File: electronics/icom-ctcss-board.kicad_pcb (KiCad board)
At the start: 2 copper layers, 100 x 150 mm, 42 parts, among them J1 J_MIC_IN, J2 J_RADIO_OUT, J3 J_UI_ENCODER, J4 J_UI_LCD, J5 J_BYPASS, J6 J_UI_LEDS, Q1 2N3904RLRAG, U1 Teyleten USB-C 5V/16MHz

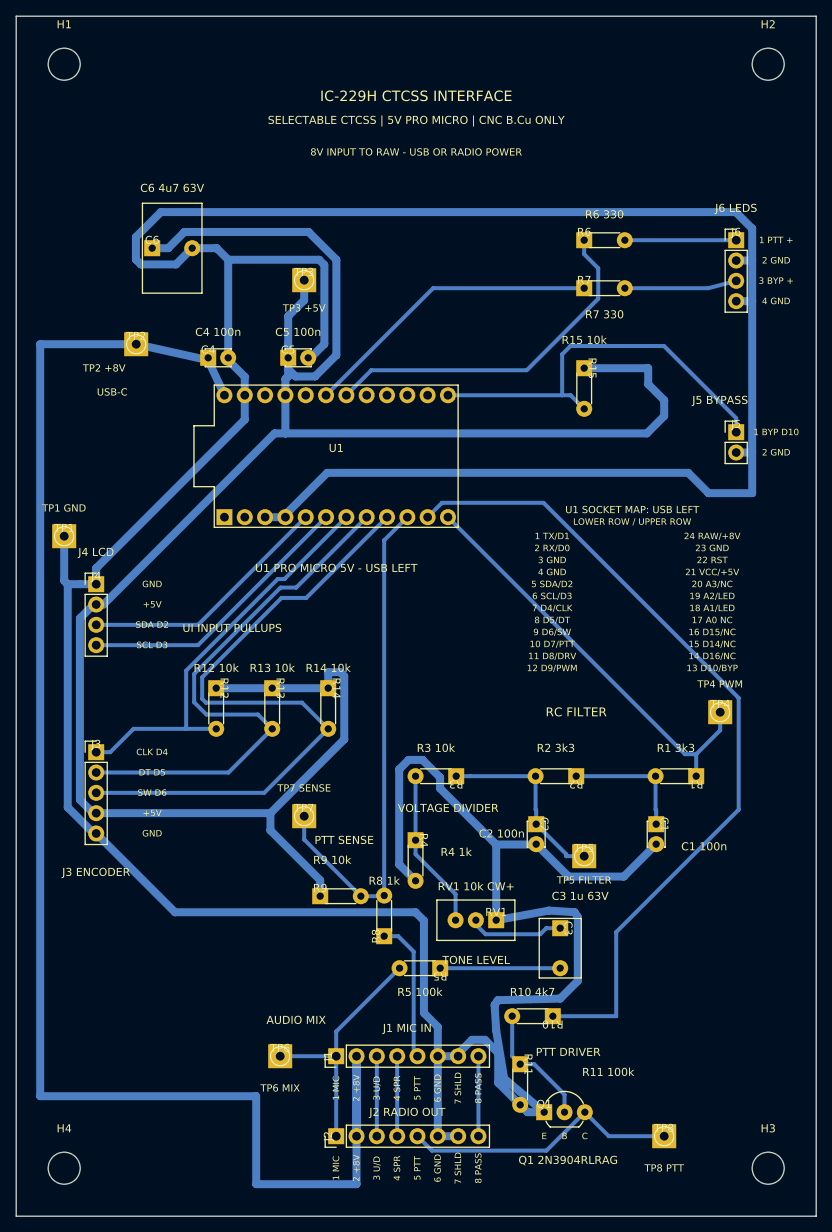
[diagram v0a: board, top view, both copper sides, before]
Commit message: updates due to parts availability
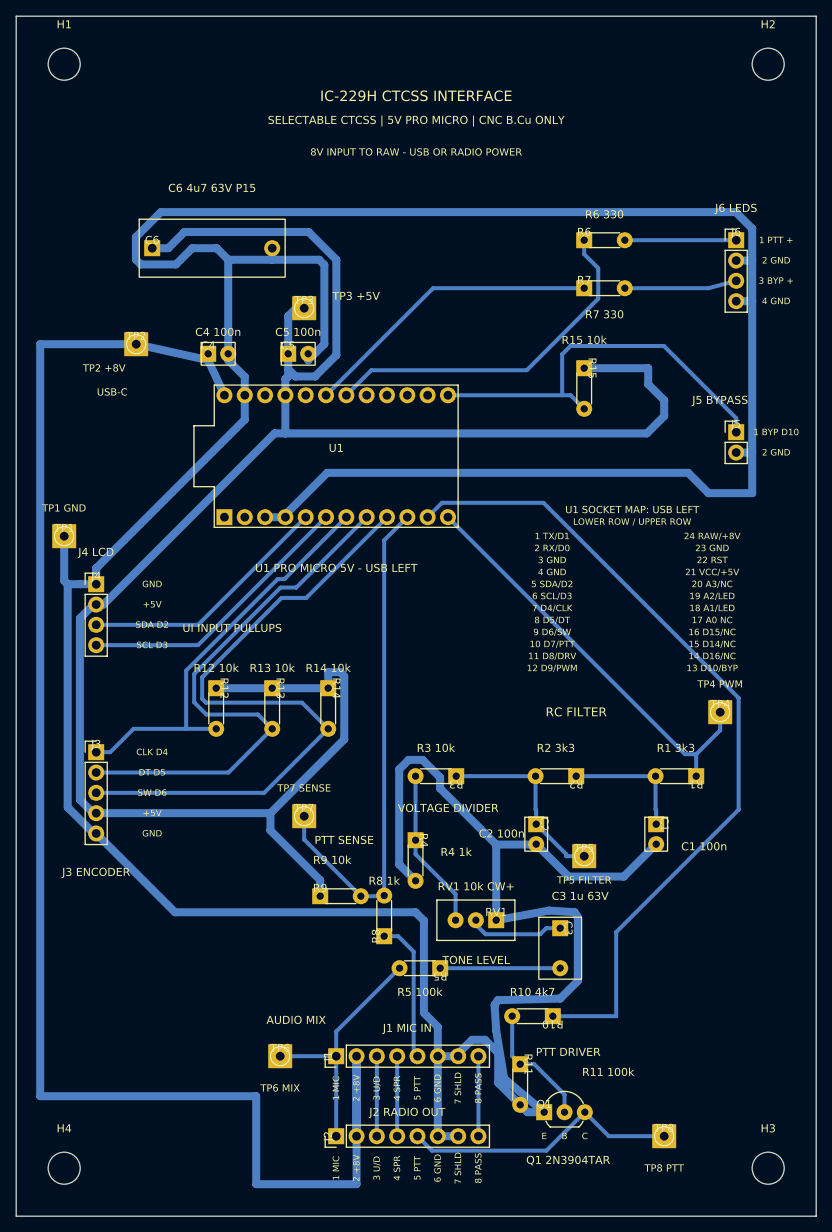
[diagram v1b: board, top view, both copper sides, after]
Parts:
- C6: footprint CTCSS_THT:C_Film4u7_P5_CNC -> CTCSS_THT:C_Film4u7_P15_CNC
- Q1: value 2N3904RLRAG -> 2N3904TAR
- moved TP3 3.50 mm to (86.0, 86.5)
- moved C4 0.50 mm to (74.0, 92.2)
- moved C5 0.50 mm to (84.0, 92.2)
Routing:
- net +5V: track 262.8 -> 261.3 mm
- net GND: track 523.5 -> 524.9 mm
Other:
- board text added: "C6 4u7 63V P15"
- board text added: "Q1 2N3904TAR"
- board text removed: "C6 4u7 63V"
- board text removed: "Q1 2N3904RLRAG"

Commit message: incorporates new jig
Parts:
- added H5: JigRegistration_4.03mm, CTCSS_THT:JigRegistration_4.03mm, F.Cu at (70.0, 70.0)
- added H6: JigRegistration_4.03mm, CTCSS_THT:JigRegistration_4.03mm, F.Cu at (70.0, 180.0)
- added H7: JigRegistration_4.12mm, CTCSS_THT:JigRegistration_4.12mm, F.Cu at (120.0, 70.0)
- added H8: JigRegistration_4.12mm, CTCSS_THT:JigRegistration_4.12mm, F.Cu at (120.0, 180.0)
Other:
- board text added: "JIG P1=H5 P2=H6 P3=H7 P4=H8 | PANEL x=Ky-50 y=Kx-50 | FLIP x'=150-x"
